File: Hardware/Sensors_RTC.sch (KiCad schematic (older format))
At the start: 9 parts

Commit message: [Hardware] Added RTC battery and Adafruit BME680 board.
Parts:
- added BT1: Battery, Battery:BatteryHolder_Keystone_103_1x20mm, symbol Device:Battery
- added U3: Adafruit_BME680, Symbol:Symbol_Attention_CopperTop_Small, symbol Adafruit_BME680:Adafruit_BME680
- C1, C2, C3: renamed from C?; Champ4 (none) -> 25V; Valeur4 16V -> (none)
- H1, H2: renamed from H?; footprint (none) -> MountingHole:MountingHole_2.7mm_Pad
- J1: renamed from J?; footprint (none) -> Connector_PinHeader_2.54mm:PinHeader_1x07_P2.54mm_Vertical
- gave numbers to parts that had none: 3
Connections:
- net GND: now also BT1.2 (-)
- net at U2.14 (VBAT): now also BT1.1 (+)
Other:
- note removed: "TODO VBAT"
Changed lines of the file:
@@
 EESchema Schematic File Version 4
+LIBS:Motherboard-cache
 EELAYER 30 0
 EELAYER END
@@
 P 8150 2350
 AR Path="/5E7B014E" Ref="H?"  Part="1"
-AR Path="/5E7ACE5B/5E7B014E" Ref="H?"  Part="1"
-F 0 "H?" H 8250 2399 50  0000 L CNN
+AR Path="/5E7ACE5B/5E7B014E" Ref="H1"  Part="1"
+F 0 "H1" H 8250 2399 50  0000 L CNN
 F 1 "MountingHole_Pad" H 8250 2308 50  0000 L CNN
-F 2 "" H 8150 2350 50  0001 C CNN
+F 2 "MountingHole:MountingHole_2.7mm_Pad" H 8150 2350 50  0001 C CNN
 F 3 "~" H 8150 2350 50  0001 C CNN
 	1    8150 2350
@@
 P 9150 2350
 AR Path="/5E7B0154" Ref="H?"  Part="1"
-AR Path="/5E7ACE5B/5E7B0154" Ref="H?"  Part="1"
-F 0 "H?" H 9250 2399 50  0000 L CNN
+AR Path="/5E7ACE5B/5E7B0154" Ref="H2"  Part="1"
+F 0 "H2" H 9250 2399 50  0000 L CNN
 F 1 "MountingHole_Pad" H 9250 2308 50  0000 L CNN
-F 2 "" H 9150 2350 50  0001 C CNN
+F 2 "MountingHole:MountingHole_2.7mm_Pad" H 9150 2350 50  0001 C CNN
 F 3 "~" H 9150 2350 50  0001 C CNN
 	1    9150 2350
@@
 P 8650 2850
 AR Path="/5E7B015A" Ref="J?"  Part="1"
-AR Path="/5E7ACE5B/5E7B015A" Ref="J?"  Part="1"
-F 0 "J?" V 8485 2828 50  0000 C CNN
+AR Path="/5E7ACE5B/5E7B015A" Ref="J1"  Part="1"
+F 0 "J1" V 8485 2828 50  0000 C CNN
 F 1 "Conn_01x07_Male" V 8576 2828 50  0000 C CNN
-F 2 "" H 8650 2850 50  0001 C CNN
+F 2 "Connector_PinHeader_2.54mm:PinHeader_1x07_P2.54mm_Vertical" H 8650 2850 50  0001 C CNN
 F 3 "~" H 8650 2850 50  0001 C CNN
 	1    8650 2850
@@
 P 8350 3400
 AR Path="/5E7B0165" Ref="#PWR?"  Part="1"
-AR Path="/5E7ACE5B/5E7B0165" Ref="#PWR?"  Part="1"
-F 0 "#PWR?" H 8350 3250 50  0001 C CNN
+AR Path="/5E7ACE5B/5E7B0165" Ref="#PWR0101"  Part="1"
+F 0 "#PWR0101" H 8350 3250 50  0001 C CNN
 F 1 "+5V" H 8365 3573 50  0000 C CNN
 F 2 "" H 8350 3400 50  0001 C CNN
@@
 P 8550 3400
 AR Path="/5E7B016B" Ref="#PWR?"  Part="1"
-AR Path="/5E7ACE5B/5E7B016B" Ref="#PWR?"  Part="1"
-F 0 "#PWR?" H 8550 3150 50  0001 C CNN
+AR Path="/5E7ACE5B/5E7B016B" Ref="#PWR0102"  Part="1"
+F 0 "#PWR0102" H 8550 3150 50  0001 C CNN
 F 1 "GND" H 8555 3227 50  0000 C CNN
 F 2 "" H 8550 3400 50  0001 C CNN
@@
 P 8150 2550
 AR Path="/5E7B0172" Ref="#PWR?"  Part="1"
-AR Path="/5E7ACE5B/5E7B0172" Ref="#PWR?"  Part="1"
-F 0 "#PWR?" H 8150 2300 50  0001 C CNN
+AR Path="/5E7ACE5B/5E7B0172" Ref="#PWR0103"  Part="1"
+F 0 "#PWR0103" H 8150 2300 50  0001 C CNN
 F 1 "GND" H 8155 2377 50  0000 C CNN
 F 2 "" H 8150 2550 50  0001 C CNN
@@
 P 9150 2550
 AR Path="/5E7B0178" Ref="#PWR?"  Part="1"
-AR Path="/5E7ACE5B/5E7B0178" Ref="#PWR?"  Part="1"
-F 0 "#PWR?" H 9150 2300 50  0001 C CNN
+AR Path="/5E7ACE5B/5E7B0178" Ref="#PWR0104"  Part="1"
+F 0 "#PWR0104" H 9150 2300 50  0001 C CNN
 F 1 "GND" H 9155 2377 50  0000 C CNN
 F 2 "" H 9150 2550 50  0001 C CNN
@@
 	8350 3050 8350 3300
 $Comp
-L Timer_RTC:DS3231M U?
+L Timer_RTC:DS3231M U2
 U 1 1 5E7B0716
 P 3450 4000
-F 0 "U?" H 3650 3650 50  0000 C CNN
+F 0 "U2" H 3650 3650 50  0000 C CNN
 F 1 "DS3231M" H 3750 3550 50  0000 C CNN
 F 2 "Package_SO:SOIC-16W_7.5x10.3mm_P1.27mm" H 3450 3400 50  0001 C CNN
@@
 P 3350 2950
 AR Path="/5E7B71D3" Ref="#PWR?"  Part="1"
-AR Path="/5E7ACE5B/5E7B71D3" Ref="#PWR?"  Part="1"
-F 0 "#PWR?" H 3350 2800 50  0001 C CNN
+AR Path="/5E7ACE5B/5E7B71D3" Ref="#PWR0105"  Part="1"
+F 0 "#PWR0105" H 3350 2800 50  0001 C CNN
 F 1 "+5V" H 3365 3123 50  0000 C CNN
 F 2 "" H 3350 2950 50  0001 C CNN
@@
 $EndComp
 $Comp
-L Device:C C?
+L Device:C C1
 U 1 1 5E7B7D0E
 P 2400 3250
-F 0 "C?" H 2285 3113 50  0000 R CNN
+F 0 "C1" H 2285 3113 50  0000 R CNN
 F 1 "100n" H 2285 3204 50  0000 R CNN
 F 2 "Capacitor_SMD:C_1206_3216Metric_Pad1.42x1.75mm_HandSolder" H 2438 3100 50  0001 C CNN
 F 3 "~" H 2400 3250 50  0001 C CNN
-F 4 "16V" H 2285 3295 50  0000 R CNN "Valeur4"
+F 4 "25V" H 2285 3295 50  0000 R CNN "Champ4"
 F 5 "X7R" H 2285 3386 50  0000 R CNN "Champ5"
 	1    2400 3250
@@
 P 3450 4450
 AR Path="/5E7BA8C5" Ref="#PWR?"  Part="1"
-AR Path="/5E7ACE5B/5E7BA8C5" Ref="#PWR?"  Part="1"
-F 0 "#PWR?" H 3450 4200 50  0001 C CNN
+AR Path="/5E7ACE5B/5E7BA8C5" Ref="#PWR0106"  Part="1"
+F 0 "#PWR0106" H 3450 4200 50  0001 C CNN
 F 1 "GND" H 3455 4277 50  0000 C CNN
 F 2 "" H 3450 4450 50  0001 C CNN
@@
 $EndComp
 $Comp
-L Device:C C?
+L Device:C C2
 U 1 1 5E7BB22C
 P 2900 3250
-F 0 "C?" H 2785 3113 50  0000 R CNN
+F 0 "C2" H 2785 3113 50  0000 R CNN
 F 1 "100n" H 2785 3204 50  0000 R CNN
 F 2 "Capacitor_SMD:C_1206_3216Metric_Pad1.42x1.75mm_HandSolder" H 2938 3100 50  0001 C CNN
 F 3 "~" H 2900 3250 50  0001 C CNN
-F 4 "16V" H 2785 3295 50  0000 R CNN "Valeur4"
+F 4 "25V" H 2785 3295 50  0000 R CNN "Champ4"
 F 5 "X7R" H 2785 3386 50  0000 R CNN "Champ5"
 	1    2900 3250
@@
 $EndComp
 $Comp
-L Device:R R?
+L Device:R R2
 U 1 1 5E7BCF59
 P 2600 4200
-F 0 "R?" H 2670 4246 50  0000 L CNN
+F 0 "R2" H 2670 4246 50  0000 L CNN
 F 1 "1K" H 2670 4155 50  0000 L CNN
 F 2 "Resistor_SMD:R_1206_3216Metric_Pad1.42x1.75mm_HandSolder" V 2530 4200 50  0001 C CNN
@@
 $EndComp
 $Comp
-L Device:R R?
+L Device:R R1
 U 1 1 5E7BE463
 P 2200 4200
-F 0 "R?" H 2270 4246 50  0000 L CNN
+F 0 "R1" H 2270 4246 50  0000 L CNN
 F 1 "1K" H 2270 4155 50  0000 L CNN
 F 2 "Resistor_SMD:R_1206_3216Metric_Pad1.42x1.75mm_HandSolder" V 2130 4200 50  0001 C CNN
@@
 P 2650 3500
 AR Path="/5E7BE8CF" Ref="#PWR?"  Part="1"
-AR Path="/5E7ACE5B/5E7BE8CF" Ref="#PWR?"  Part="1"
-F 0 "#PWR?" H 2650 3250 50  0001 C CNN
+AR Path="/5E7ACE5B/5E7BE8CF" Ref="#PWR0107"  Part="1"
+F 0 "#PWR0107" H 2650 3250 50  0001 C CNN
 F 1 "GND" H 2655 3327 50  0000 C CNN
 F 2 "" H 2650 3500 50  0001 C CNN
@@
 P 2400 4450
 AR Path="/5E7C118A" Ref="#PWR?"  Part="1"
-AR Path="/5E7ACE5B/5E7C118A" Ref="#PWR?"  Part="1"
-F 0 "#PWR?" H 2400 4300 50  0001 C CNN
+AR Path="/5E7ACE5B/5E7C118A" Ref="#PWR0108"  Part="1"
+F 0 "#PWR0108" H 2400 4300 50  0001 C CNN
 F 1 "+5V" H 2415 4623 50  0000 C CNN
 F 2 "" H 2400 4450 50  0001 C CNN
@@
 Text HLabel 1650 3900 0    50   BiDi ~ 0
 RTC_SDA
-Text Notes 3650 3400 0    315  ~ 63
-TODO VBAT
 Wire Wire Line
 	8650 4350 7700 4350
@@
 	8950 4650 7700 4650
 $Comp
-L Device:C C?
+L Device:C C3
 U 1 1 5E7D259F
 P 7900 3500
-F 0 "C?" H 7785 3363 50  0000 R CNN
+F 0 "C3" H 7785 3363 50  0000 R CNN
 F 1 "100n" H 7785 3454 50  0000 R CNN
 F 2 "Capacitor_SMD:C_1206_3216Metric_Pad1.42x1.75mm_HandSolder" H 7938 3350 50  0001 C CNN
 F 3 "~" H 7900 3500 50  0001 C CNN
-F 4 "16V" H 7785 3545 50  0000 R CNN "Valeur4"
+F 4 "25V" H 7785 3545 50  0000 R CNN "Champ4"
 F 5 "X7R" H 7785 3636 50  0000 R CNN "Champ5"
 	1    7900 3500
@@
 P 7900 3750
 AR Path="/5E7E1118" Ref="#PWR?"  Part="1"
-AR Path="/5E7ACE5B/5E7E1118" Ref="#PWR?"  Part="1"
-F 0 "#PWR?" H 7900 3500 50  0001 C CNN
+AR Path="/5E7ACE5B/5E7E1118" Ref="#PWR0109"  Part="1"
+F 0 "#PWR0109" H 7900 3500 50  0001 C CNN
 F 1 "GND" H 7905 3577 50  0000 C CNN
 F 2 "" H 7900 3750 50  0001 C CNN
@@
 Text HLabel 7700 4650 0    50   Input ~ 0
 BME680_CS
+$Comp
+L Adafruit_BME680:Adafruit_BME680 U3
+U 1 1 5E7A3D1F
+P 8600 1250
+F 0 "U3" H 9028 1296 50  0000 L CNN
+F 1 "Adafruit_BME680" H 9028 1205 50  0000 L CNN
+F 2 "Symbol:Symbol_Attention_CopperTop_Small" H 8600 1250 50  0001 C CNN
+F 3 "" H 8600 1250 50  0001 C CNN
+	1    8600 1250
+	1    0    0    -1
+$EndComp
+$Comp
+L Device:Battery BT1
+U 1 1 5E7A7D04
+P 4300 3700
+F 0 "BT1" H 4408 3746 50  0000 L CNN
+F 1 "Battery" H 4408 3655 50  0000 L CNN
+F 2 "Battery:BatteryHolder_Keystone_103_1x20mm" V 4300 3760 50  0001 C CNN
+F 3 "~" V 4300 3760 50  0001 C CNN
+	1    4300 3700
+	1    0    0    -1
+$EndComp
+$Comp
+L power:GND #PWR?
+U 1 1 5E7AC503
+P 4300 4000
+AR Path="/5E7AC503" Ref="#PWR?"  Part="1"
+AR Path="/5E7ACE5B/5E7AC503" Ref="#PWR0110"  Part="1"
+F 0 "#PWR0110" H 4300 3750 50  0001 C CNN
+F 1 "GND" H 4305 3827 50  0000 C CNN
+F 2 "" H 4300 4000 50  0001 C CNN
+F 3 "" H 4300 4000 50  0001 C CNN
+	1    4300 4000
+	1    0    0    -1
+$EndComp
+Wire Wire Line
+	3450 3600 3450 3450
+Wire Wire Line
+	3450 3450 4300 3450
+Wire Wire Line
+	4300 3450 4300 3500
+Wire Wire Line
+	4300 3900 4300 4000
 $EndSCHEMATC

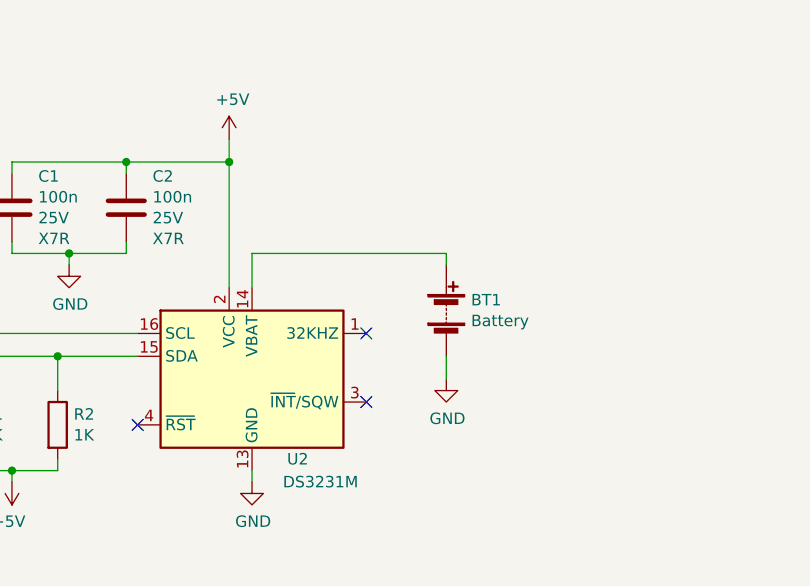
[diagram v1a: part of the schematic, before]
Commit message: [Hardware] Replaced PIC18F26K22 microcontroller by PIC18F46K22 to have more pins.
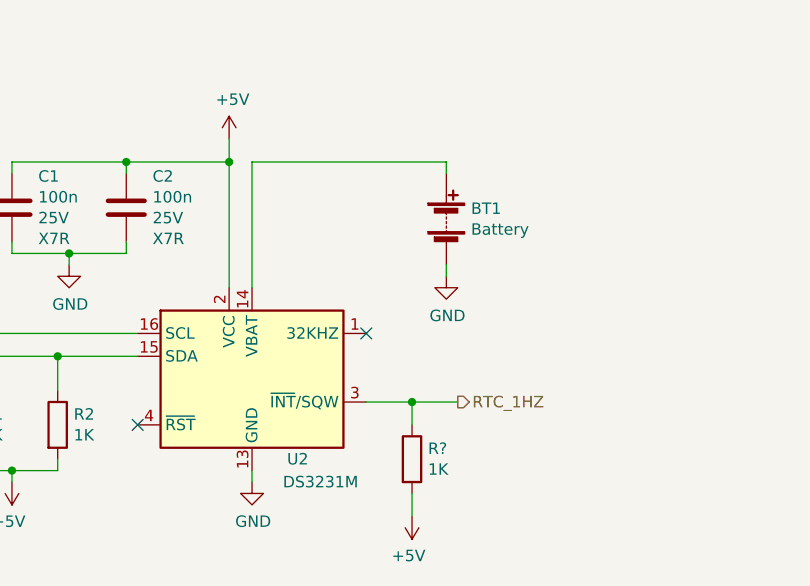
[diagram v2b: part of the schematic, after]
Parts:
- added R?: 1K, Resistor_SMD:R_1206_3216Metric_Pad1.42x1.75mm_HandSolder, symbol Device:R
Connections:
- net +5V: now also R?.2
- net RTC_1HZ: now reaches U2.3 (~INT~/SQW)
- net RTC_1HZ: now also R?.1
- no-connect marks 4 -> 3
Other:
- moved on the sheet: BT1
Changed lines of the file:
@@
 Wire Wire Line
 	3450 4450 3450 4400
-NoConn ~ 3950 4100
 NoConn ~ 3950 3800
 Text HLabel 1650 3800 0    50   Input ~ 0
@@
 L Device:Battery BT1
 U 1 1 5E7A7D04
-P 4300 3700
-F 0 "BT1" H 4408 3746 50  0000 L CNN
-F 1 "Battery" H 4408 3655 50  0000 L CNN
-F 2 "Battery:BatteryHolder_Keystone_103_1x20mm" V 4300 3760 50  0001 C CNN
-F 3 "~" V 4300 3760 50  0001 C CNN
-	1    4300 3700
+P 4300 3300
+F 0 "BT1" H 4408 3346 50  0000 L CNN
+F 1 "Battery" H 4408 3255 50  0000 L CNN
+F 2 "Battery:BatteryHolder_Keystone_103_1x20mm" V 4300 3360 50  0001 C CNN
+F 3 "~" V 4300 3360 50  0001 C CNN
+	1    4300 3300
 	1    0    0    -1
 $EndComp
@@
 L power:GND #PWR?
 U 1 1 5E7AC503
-P 4300 4000
+P 4300 3550
 AR Path="/5E7AC503" Ref="#PWR?"  Part="1"
 AR Path="/5E7ACE5B/5E7AC503" Ref="#PWR0110"  Part="1"
-F 0 "#PWR0110" H 4300 3750 50  0001 C CNN
-F 1 "GND" H 4305 3827 50  0000 C CNN
-F 2 "" H 4300 4000 50  0001 C CNN
-F 3 "" H 4300 4000 50  0001 C CNN
-	1    4300 4000
+F 0 "#PWR0110" H 4300 3300 50  0001 C CNN
+F 1 "GND" H 4305 3377 50  0000 C CNN
+F 2 "" H 4300 3550 50  0001 C CNN
+F 3 "" H 4300 3550 50  0001 C CNN
+	1    4300 3550
 	1    0    0    -1
 $EndComp
 Wire Wire Line
-	3450 3600 3450 3450
+	3450 3050 4300 3050
 Wire Wire Line
-	3450 3450 4300 3450
+	4300 3050 4300 3100
 Wire Wire Line
-	4300 3450 4300 3500
+	4300 3500 4300 3550
 Wire Wire Line
-	4300 3900 4300 4000
+	3450 3050 3450 3600
+Text HLabel 4350 4100 2    50   Output ~ 0
+RTC_1HZ
+$Comp
+L Device:R R?
+U 1 1 5E7E2482
+P 4150 4350
+F 0 "R?" H 4220 4396 50  0000 L CNN
+F 1 "1K" H 4220 4305 50  0000 L CNN
+F 2 "Resistor_SMD:R_1206_3216Metric_Pad1.42x1.75mm_HandSolder" V 4080 4350 50  0001 C CNN
+F 3 "~" H 4150 4350 50  0001 C CNN
+	1    4150 4350
+	1    0    0    -1
+$EndComp
+$Comp
+L power:+5V #PWR?
+U 1 1 5E7E2996
+P 4150 4600
+AR Path="/5E7E2996" Ref="#PWR?"  Part="1"
+AR Path="/5E7ACE5B/5E7E2996" Ref="#PWR?"  Part="1"
+F 0 "#PWR?" H 4150 4450 50  0001 C CNN
+F 1 "+5V" H 4165 4773 50  0000 C CNN
+F 2 "" H 4150 4600 50  0001 C CNN
+F 3 "" H 4150 4600 50  0001 C CNN
+	1    4150 4600
+	-1   0    0    1
+$EndComp
+Wire Wire Line
+	4150 4200 4150 4100
+Connection ~ 4150 4100
+Wire Wire Line
+	4150 4100 4350 4100
+Wire Wire Line
+	4150 4600 4150 4500
+Wire Wire Line
+	3950 4100 4150 4100
 $EndSCHEMATC

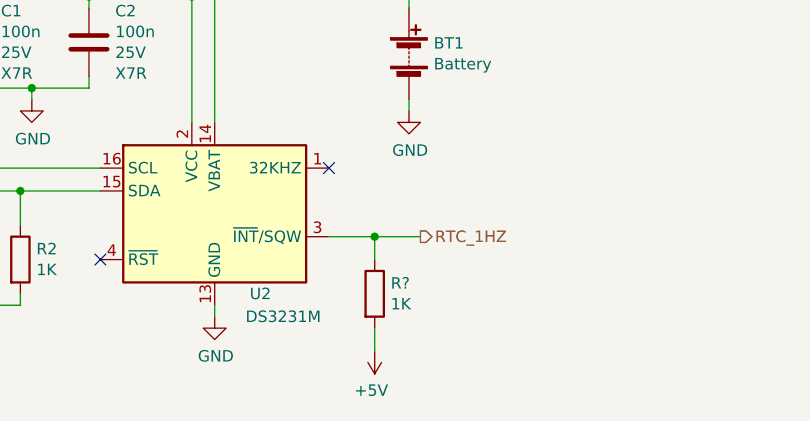
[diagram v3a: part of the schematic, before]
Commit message: [Hardware] Added buttons.
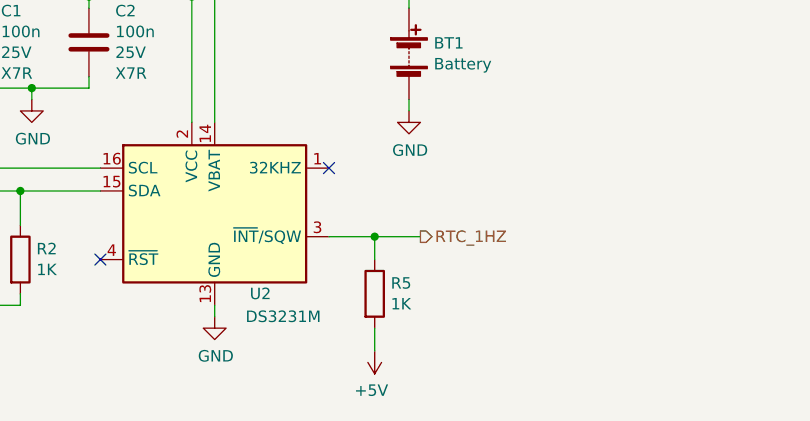
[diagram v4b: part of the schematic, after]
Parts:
- gave numbers to parts that had none: 1
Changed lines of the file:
@@
 RTC_1HZ
 $Comp
-L Device:R R?
+L Device:R R5
 U 1 1 5E7E2482
 P 4150 4350
-F 0 "R?" H 4220 4396 50  0000 L CNN
+F 0 "R5" H 4220 4396 50  0000 L CNN
 F 1 "1K" H 4220 4305 50  0000 L CNN
 F 2 "Resistor_SMD:R_1206_3216Metric_Pad1.42x1.75mm_HandSolder" V 4080 4350 50  0001 C CNN
@@
 P 4150 4600
 AR Path="/5E7E2996" Ref="#PWR?"  Part="1"
-AR Path="/5E7ACE5B/5E7E2996" Ref="#PWR?"  Part="1"
-F 0 "#PWR?" H 4150 4450 50  0001 C CNN
+AR Path="/5E7ACE5B/5E7E2996" Ref="#PWR0118"  Part="1"
+F 0 "#PWR0118" H 4150 4450 50  0001 C CNN
 F 1 "+5V" H 4165 4773 50  0000 C CNN
 F 2 "" H 4150 4600 50  0001 C CNN

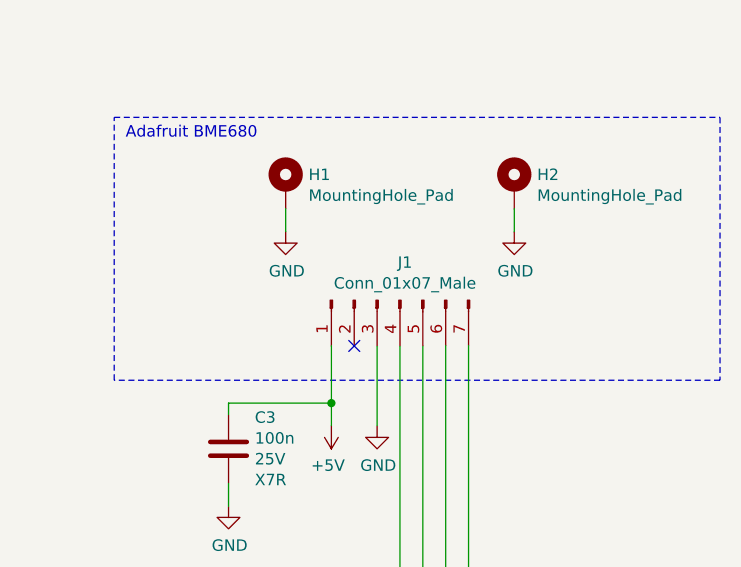
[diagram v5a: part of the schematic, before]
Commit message: [Hardware] Started PCB routing. Components are placed, BME680 board mounting holes are in position, some nets are connected.
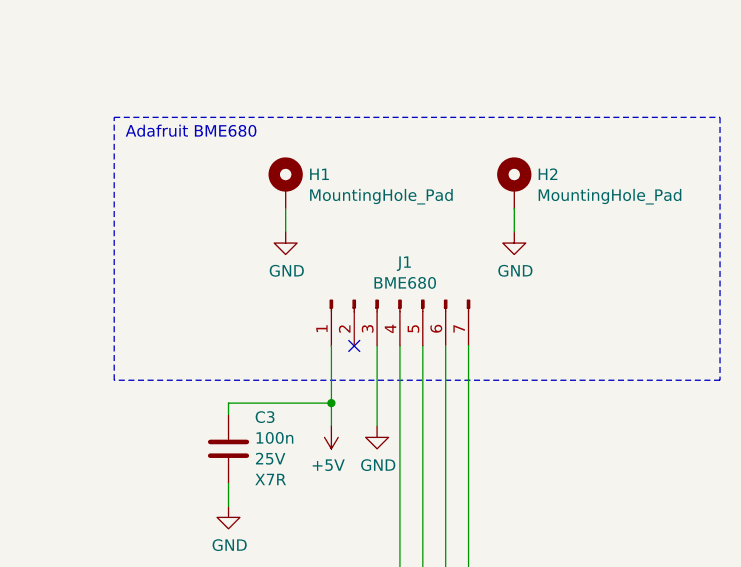
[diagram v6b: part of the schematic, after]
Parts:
- J1: value Conn_01x07_Male -> BME680
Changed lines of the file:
@@
 AR Path="/5E7ACE5B/5E7B015A" Ref="J1"  Part="1"
 F 0 "J1" V 8485 2828 50  0000 C CNN
-F 1 "Conn_01x07_Male" V 8576 2828 50  0000 C CNN
+F 1 "BME680" V 8576 2828 50  0000 C CNN
 F 2 "Connector_PinHeader_2.54mm:PinHeader_1x07_P2.54mm_Vertical" H 8650 2850 50  0001 C CNN
 F 3 "~" H 8650 2850 50  0001 C CNN

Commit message: [Hardware] Used a custom empty footprint for Adafruit module part. This way, part is visible in schematic and bill of materials, but it is not part of the PCB.
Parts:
- U3: footprint Symbol:Symbol_Attention_CopperTop_Small -> Empty_Footprint:Empty_Footprint
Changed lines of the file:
@@
 F 0 "U3" H 9028 1296 50  0000 L CNN
 F 1 "Adafruit_BME680" H 9028 1205 50  0000 L CNN
-F 2 "Symbol:Symbol_Attention_CopperTop_Small" H 8600 1250 50  0001 C CNN
+F 2 "Empty_Footprint:Empty_Footprint" H 8600 1250 50  0001 C CNN
 F 3 "" H 8600 1250 50  0001 C CNN
 	1    8600 1250
